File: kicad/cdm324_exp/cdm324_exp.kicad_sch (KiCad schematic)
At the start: 29 parts, among them J3 USB_C_Receptacle_USB2.0, J4 Conn_02x04_Odd_Even, J5 Conn_02x04_Odd_Even, J5 Micro_SD_Card_Det1, J6 Conn_01x04_Socket, J7 AudioJack4, SW1 SW_Push, SW2 SW_Push, SW3 SW_DIP_x01, U1 CH340X

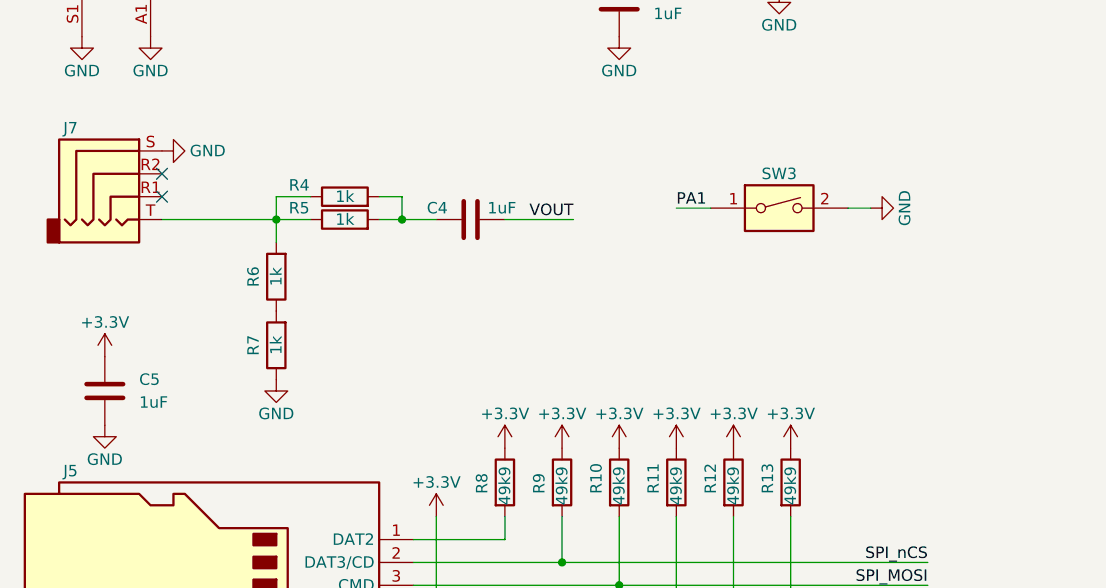
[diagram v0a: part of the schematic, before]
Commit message: correct resistor divider for jack output
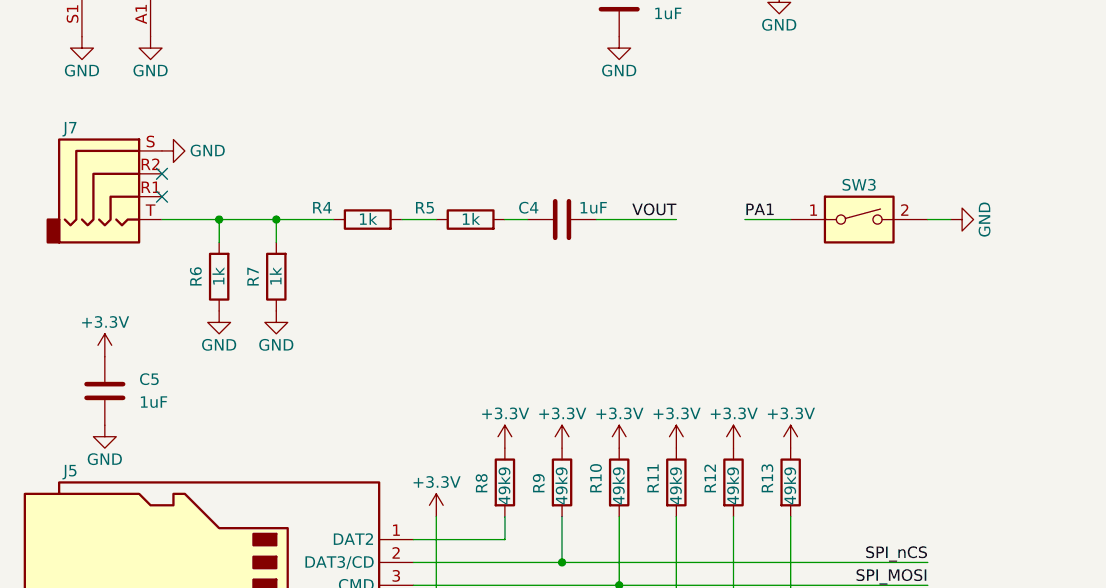
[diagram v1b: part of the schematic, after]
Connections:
- net GND: now also R6.1
- net at J7.T, R4.1, R6.2: now also R7.2; no longer R5.1
- net at C4.1, R5.2: no longer R4.2
- new net: R4.2, R5.1
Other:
- moved on the sheet: C4, R4, R5, R6, R7, SW3
